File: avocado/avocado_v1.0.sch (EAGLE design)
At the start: 35 parts, among them IC1 TM4C129XXXPDT, IC2 OP-AMP

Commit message: finished wiring MCU
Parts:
- added C15: 3300pF, SparkFun-Capacitors:1.0UF-0805-25V-(+80/-20%)
- added C16, C17, C18, C19, C20, C26, C27, C28, C29, C30: 0.1uF, SparkFun-Capacitors:1.0UF-0805-25V-10%
- added C21: 2.2uF, SparkFun-Capacitors:1.0UF-0805-25V-10%
- added C22, C23, C24, C25: 12pF, SparkFun-Capacitors:1.0UF-0805-25V-10%
- added D1: GREEN, SparkFun-LED:LED-GREEN0603
- added R12, R22: 1M, rcl:R-US_R0805
- added R13, R17: 100, rcl:R-US_R0805
- added R14: 2K, rcl:R-US_R0805
- added R18: 10K, rcl:R-US_R0805
- added R21: 51, rcl:R-US_R0805
- added R23: 0, rcl:R-US_R0805
- added R24: 4.87K 1%, rcl:R-US_R0805
- added R25: (no value), rcl:R-US_R0805
- added R26: 330, rcl:R-US_R0805
- added RESET, WAKE: B3S-10XX, avocado:B3S-10XX
- added U$7: MICRO-USB-RECEPTACLE47589-0001, avocado:MICRO-USB-RECEPTACLE47589-0001
- added U$8: CX3225SB, avocado:CX3225SB
- added U1: TPD4S012_DRY_6, avocado:TPD4S012_DRY_6
- added X1: (no value), avocado:CRYSTAL-4PIN
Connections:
- net N$100 renamed PB2
- net N$101 renamed PB3
- net N$106 renamed PD7
- net N$107 renamed PD6
- net N$108 renamed PD5
- net N$109 renamed PD4
- net N$11 renamed PQ0
- net N$110 renamed PE5
- net N$111 renamed PE4
- net N$113 renamed PB4
- net N$114 renamed PB5
- net N$115 renamed PP1
- net N$116 renamed PP0
- net N$117 renamed PJ1
- net N$118 renamed PJ0
- net N$12 renamed PQ1
- net N$122 renamed PN5
- net N$123 renamed PN4
- net N$124 renamed PN3
- net N$125 renamed PN2
- net N$126 renamed PN1
- net N$127 renamed PN0
- net N$128 renamed PP5
- net N$129 renamed PP4
- net N$130 renamed PP3
- net N$131 renamed PP2
- net N$132 renamed PQ4
- net N$134 renamed SWCLK
- net N$135 renamed SWDIO
- net N$136 renamed TDI
- net N$137 renamed SWO
- net N$17 renamed PQ2
- net N$2 renamed PD0
- net N$21 renamed PE3
- net N$22 renamed PE2
- net N$23 renamed PE1
- net N$24 renamed PE0
- net N$27 renamed PK0
- net N$28 renamed PK1
- net N$29 renamed PK2
- net N$30 renamed PK3
- net N$31 renamed PC7
- net N$32 renamed PC6
- net N$33 renamed PC5
- net N$34 renamed PC4
- net N$36 renamed PQ3
- net N$38 renamed PH0
- net N$39 renamed PH1
- net N$4 renamed PD1
- net N$40 renamed PH2
- net N$41 renamed PH3
- net N$42 renamed PA0
- net N$43 renamed PA1
- net N$44 renamed PA2
- net N$45 renamed PA3
- net N$46 renamed PA4
- net N$47 renamed PA5
- net N$49 renamed PA6
- net N$50 renamed PA7
- net N$51 renamed PF0
- net N$52 renamed PF1
- net N$53 renamed PF2
- net N$54 renamed PF3
- net N$55 renamed PF4
- net N$58 renamed PG0
- net N$59 renamed PG1
- net N$6 renamed PD2
- net N$62 renamed EN0RXIN
- net N$63 renamed EN0RXIP
- net N$65 renamed EN0TXON
- net N$66 renamed EN0TXOP
- net N$69 renamed PK7
- net N$70 renamed PK6
- net N$71 renamed PK5
- net N$72 renamed PK4
- net N$74 renamed NHIB
- net N$80 renamed PM7
- net N$81 renamed PM6
- net N$82 renamed PM5
- net N$83 renamed PM4
- net N$84 renamed PM3
- net N$85 renamed PM2
- net N$86 renamed PM1
- net N$87 renamed PM0
- net N$9 renamed PD3
- net N$90 renamed PL0
- net N$91 renamed PL1
- net N$92 renamed PL2
- net N$93 renamed PL3
- net N$94 renamed PL4
- net N$95 renamed PL5
- removed net N$102: IC1.PL7
- removed net N$103: IC1.PL6
- removed net N$104: IC1.PB0
- removed net N$112: IC1.VDD@11
- removed net N$119: IC1.VDDC@1
- removed net N$120: IC1.GND@5
- removed net N$121: IC1.VDD@12
- removed net N$13: IC1.VDD@10
- removed net N$133: IC1.VDD@13
- removed net N$14: IC1.VDDA
- removed net N$15: IC1.VREFA+
- removed net N$16: IC1.GNDA
- removed net N$25: IC1.VDD@9
- removed net N$26: IC1.GND@4
- removed net N$35: IC1.VDD@8
- removed net N$37: IC1.VDD@7
- removed net N$48: IC1.VDD@6
- removed net N$56: IC1.VDD@5
- removed net N$57: IC1.GND@3
- removed net N$60: IC1.VDD@4
- removed net N$61: IC1.VDD@3
- removed net N$64: IC1.GND@2
- removed net N$67: IC1.GND@1
- removed net N$73: IC1.!WAKE
- removed net N$75: IC1.XOSC0
- removed net N$76: IC1.XOSC1
- removed net N$77: IC1.VBAT
- removed net N$78: IC1.VDD@2
- removed net N$79: IC1.!RST
- removed net N$88: IC1.VDD@1
- removed net N$89: IC1.GND
- removed net N$96: IC1.VDDC
- removed net N$97: IC1.OSC0
- removed net N$98: IC1.OSC1
- removed net N$99: IC1.VDD
- new net N$2: D1.C, R26.2
- new net N$42: C25.2
- new net N$43: R13.1, RESET.P, RESET.P1
- new net N$44: R21.1, R22.2, R23.1
- new net N$45: C24.1, R14.2, U$8.P$2
- new net N$47: C15.1, R12.2, U$7.GND1, U$7.GND2, U$7.GND3, U$7.GND4
- new net NRST: C17.1, IC1.!RST, R13.2, R18.1
- new net NWAKE: IC1.!WAKE, R22.1, WAKE.P, WAKE.P1
- new net OSC0: C25.1, IC1.OSC0, U$8.P$1
- new net OSC1: IC1.OSC1, R14.1
- new net PB0: IC1.PB1, R17.2
- new net TARGET_ID: R17.1, U$7.4, U1.D-
- new net TARGET_VBUS: IC1.PB0, U$7.1, U1.VBUS
- new net USBD_N: IC1.PL7, U$7.2, U1.D+
- new net USBD_P: IC1.PL6, U$7.3, U1.ID
- new net VBAT: C16.1, IC1.VBAT, R21.2
- new net VDDC: C21.1, C29.2, IC1.VDDC, IC1.VDDC@1
- new net VREFA: IC1.VREFA+, R25.1
- new net XOSC0: C22.1, IC1.XOSC0, X1.1
- new net XOSC1: C23.1, IC1.XOSC1, X1.4
- net 3V3DC: now also C18.1, C19.1, C20.1, C26.1, C27.2, C28.2, C30.1, D1.A, IC1.VDD, IC1.VDD@1, IC1.VDD@10, IC1.VDD@11, IC1.VDD@12, IC1.VDD@13, IC1.VDD@2, IC1.VDD@3, IC1.VDD@4, IC1.VDD@5, IC1.VDD@6, IC1.VDD@7, IC1.VDD@8, IC1.VDD@9, IC1.VDDA, R18.2, R23.2, R25.2
- net GND: now also C15.2, C16.2, C17.2, C18.2, C19.2, C20.2, C21.2, C22.2, C23.2, C24.2, C26.2, C27.1, C28.1, C29.1, C30.2, IC1.GND, IC1.GND@1, IC1.GND@2, IC1.GND@3, IC1.GND@4, IC1.GND@5, IC1.GNDA, R12.1, R24.1, R26.1, RESET.S, RESET.S1, U$7.5, U1.GND, WAKE.S, WAKE.S1
- net N$105: now also U1.N.C.; no longer IC1.PB1
- net N$68: now also R24.2
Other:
- note added: "Allen Tang Wildcat Robot Design Studio"
- note added: "BUTTONS"
- note added: "MCU"
- note added: "MOTOR"
- note added: "OSCILLATORS"
- note added: "POWER"
- note added: "USB"
- moved on the sheet: C1, C2, C3, C4, IC1, U$1, U$2

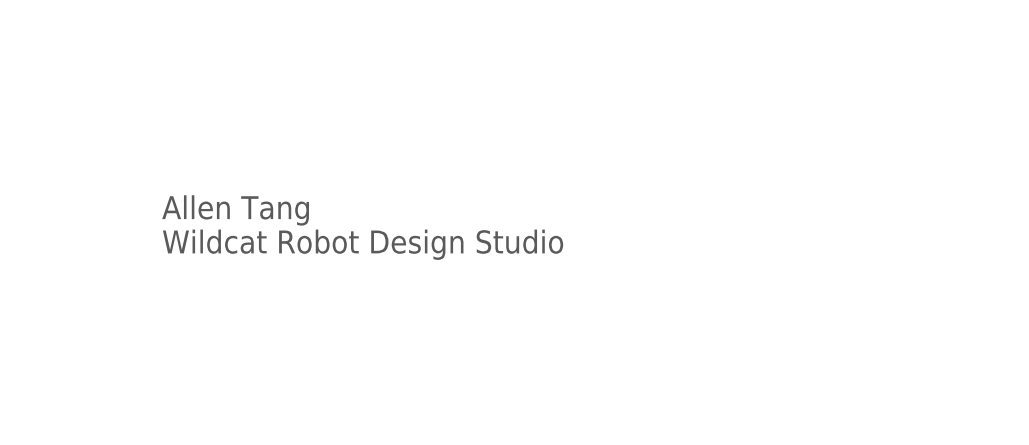
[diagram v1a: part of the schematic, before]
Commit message: fixed the title block
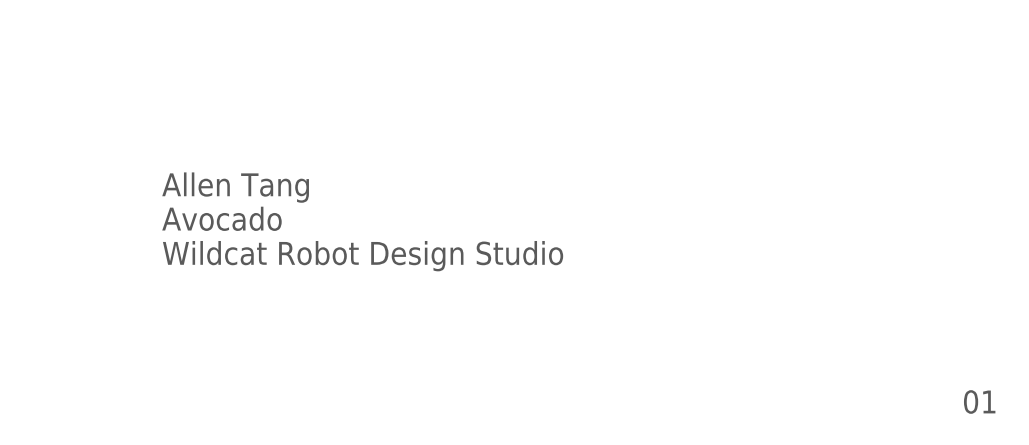
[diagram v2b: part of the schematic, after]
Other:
- note added: "01"
- note added: "Allen Tang Avocado Wildcat Robot Design Studio"
- note removed: "Allen Tang Wildcat Robot Design Studio"
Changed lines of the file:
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@@
 <wire x1="190.5" y1="81.28" x2="83.82" y2="81.28" width="0.1524" layer="97"/>
 <text x="86.36" y="78.74" size="1.778" layer="97">USB</text>
-<text x="152.4" y="-220.98" size="2.54" layer="97">Allen Tang
+<text x="152.4" y="-222.25" size="2.54" layer="97">Allen Tang
+Avocado
 Wildcat Robot Design Studio</text>
+<text x="241.3" y="-238.76" size="2.54" layer="97">01</text>
 </plain>
 <instances>

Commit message: added power and encoder block
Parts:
- removed R26: 330, rcl:R-US_R0805
- removed U$1: TLV70233DBVR, avocado:TLV70233DBVR
- removed U$2: UA78M05CDCYR, avocado:UA78M05CDCYR
- added 3V3BUCK, 5VBUCK: LM2594M-5.0, avocado:LM2594M-5.0
- added C31: 2.2uF, SparkFun-Capacitors:1.0UF-0805-25V-10%
- added C32: 1uF, SparkFun-Capacitors:1.0UF-0805-25V-10%
- added C33: 10uF, adafruit:C-USC0805K
- added C35: 0.01µF, microbuilder:CAP_CERAMIC_0805
- added D2: 1n4148, adafruit:DIODESOD-323F
- added D3: 1N4148, adafruit:DIODESOD-323F
- added D4: MBRS130LT3, avocado:MBRS130LT3
- added FB1, FB2: Ferrite, microbuilder:FERRITE_0805
- added IC3: MAX31855, adafruit:MAX6675
- added IC4: ISO3088ISO3088, avocado:ISO3088ISO3088
- added J1: 1X2-3.5MM, adafruit:1X2-3.5MM
- added OPTBIT0, OPTBIT1, OPTBIT2, OPTBIT3: (no value), avocado:QRE1113
- added R19, R27, R29, R31: 100, rcl:R-US_R0805
- added R20, R28, R30, R32: 10K, rcl:R-US_R0805
- added R33, R34: 10K, adafruit:R-US_R0805
- added SRU1028-101Y, SRU1028-151Y: SRU1028, avocado:SRU1028
- added U2: AS5048A-HTSP-500, avocado:AS5048A-HTSP-500
- C1: value 1.0uF -> 100u; device SparkFun-Capacitors:1.0UF-0805-25V-(+80/-20%) -> avocado:AVX_TPS_CAPD
- C2: value 0.33µF -> 15u; device SparkFun-Capacitors:0.33UF/330NF-0805-50V-10% -> avocado:AVX_TPS_CAPD
- C3: value 0.1uF -> 100u; device SparkFun-Capacitors:1.0UF-0805-25V-(+80/-20%) -> avocado:AVX_TPS_CAPD
- C4: value 0.1uF -> 15u; device SparkFun-Capacitors:1.0UF-0805-25V-(+80/-20%) -> avocado:AVX_TPS_CAPD
- D1: value GREEN -> MBRS130LT3; device SparkFun-LED:LED-GREEN0603 -> avocado:MBRS130LT3
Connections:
- removed net N$2: D1.C, R26.2
- removed net N$3: U$1.NC
- new net +3V3: C33.1, IC3.VCC, R33.1, R34.1
- new net CS: D3.A, IC3./CS, R34.2
- new net N$12: OPTBIT1.A, R29.1
- new net N$13: FB1.P$1, J1.2
- new net N$14: OPTBIT0.A, R31.1
- new net N$15: C35.P$1, FB1.P$2, IC3.T-
- new net N$16: FB2.P$1, J1.1
- new net N$17: C35.P$2, FB2.P$2, IC3.T+
- new net N$24: 5VBUCK.OUT, D1.C, SRU1028-151Y.1
- new net N$25: 3V3BUCK.OUT, D4.C, SRU1028-101Y.1
- new net N$26: IC4.A
- new net N$30: IC4.VCC2
- new net N$31: IC4.GND2@15
- new net N$32: IC4.B
- new net N$34: IC4.GND2@10
- new net N$35: IC4.GND2@9
- new net N$4: OPTBIT3.A, R19.1
- new net N$9: OPTBIT2.A, R27.1
- new net SCK: D2.A, IC3.SCK, R33.2
- net 24VDC: now also 3V3BUCK.VIN, 5VBUCK.VIN, C2.A, C4.A; no longer C2.1, U$2.VIN
- net 3V3DC: now also 3V3BUCK.FB, C3.A, C31.1, C32.1, IC4.VCC1, R19.2, R20.2, R27.2, R28.2, R29.2, R30.2, R31.2, R32.2, SRU1028-101Y.2, U2.VDD3V, U2.VDD5V; no longer C4.1, D1.A, U$1.VOUT
- net 5VDC: now also 5VBUCK.FB, C1.A, SRU1028-151Y.2; no longer C1.1, C3.1, U$1.VIN, U$2.VOUT
- net GND: now also 3V3BUCK.GND, 3V3BUCK.ON/OFF, 5VBUCK.GND, 5VBUCK.ON/OFF, C1.C, C2.C, C3.C, C31.2, C32.2, C33.2, C4.C, D1.A, D4.A, IC3.GND, IC4.GND1@2, IC4.GND1@7, IC4.GND1@8, OPTBIT0.E, OPTBIT0.K, OPTBIT1.E, OPTBIT1.K, OPTBIT2.E, OPTBIT2.K, OPTBIT3.E, OPTBIT3.K, U2.GND; no longer C1.2, C2.2, C3.2, C4.2, R26.1, U$1.GND, U$2.GND
- net PA2: now also U2.CLK
- net PA3: now also U2.!CSN
- net PA4: now also U2.MOSI
- net PA5: now also U2.MISO
- net PB4: now also D3.C
- net PB5: now also D2.C
- net PC4: now also IC4.R
- net PC5: now also IC4.D
- net PC6: now also IC4.!RE, IC4.DE
- net PE0: now also OPTBIT0.C, R32.1
- net PE1: now also OPTBIT1.C, R30.1
- net PE2: now also OPTBIT2.C, R28.1
- net PE3: now also OPTBIT3.C, R20.1
- net PE4: now also IC3.DO
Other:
- note added: "ENCODER"
- note added: "RS485"
- note added: "TEMPERATURE"
- moved on the sheet: C10, C11, C12, C13, C14, C15, C16, C17, C18, C19, C20, C21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

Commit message: updated motor block, power and temperature
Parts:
- removed C10: 33nF, SparkFun-Capacitors:1.0UF-0805-25V-10%
- removed C11: 5.6nF, SparkFun-Capacitors:1.0UF-0805-25V-10%
- removed C12, C7: 220nF, SparkFun-Capacitors:1.0UF-0805-25V-10%
- removed C13, C9: 10nF, SparkFun-Capacitors:1.0UF-0805-25V-10%
- removed C14, C6: 100nF, SparkFun-Capacitors:1.0UF-0805-25V-10%
- removed C15: 3300pF, SparkFun-Capacitors:1.0UF-0805-25V-(+80/-20%)
- removed C5: 100uF, SparkFun-Capacitors:100UF-POLAR-RADIAL-2.5MM-25V-20%
- removed C8: 1nF, SparkFun-Capacitors:1.0UF-0805-25V-10%
- removed IC2: OP-AMP, SparkFun-IC-Amplifiers:OPAMP-DUALDIP
- removed R10: 47K, rcl:R-US_R0805
- removed R11, R15, R16: 10, rcl:R-US_R0805
- removed R12: 1M, rcl:R-US_R0805
- removed R17, R7: 100, rcl:R-US_R0805
- removed R4: 1.8K, rcl:R-US_R0805
- removed R5: 100K, rcl:R-US_R0805
- removed R6: 1K, rcl:R-US_R0805
- removed R8: 0.6, rcl:R-US_R0805
- removed R9: 33K, rcl:R-US_R0805
- removed U$4: EC45FLAT_BLDC, avocado:EC45FLAT_BLDC
- removed U$6: 1N4148, avocado:1N4148
- removed U$7: MICRO-USB-RECEPTACLE47589-0001, avocado:MICRO-USB-RECEPTACLE47589-0001
- added CAP-0001, CAP-1114, CAP-1115, CAP-1116, CAP-1117, CAP-1118: 10nF, SparkFun-Capacitors:0.1UF-16V(+-10%)(0402)
- added CAP-0002, CAP-0119: 0.1uF, SparkFun-Capacitors:1.0UF-25V-+80/-20(0805)"
- added CAP-0003: 100nF, SparkFun-Capacitors:0.1UF-16V(+-10%)(0402)
- added CAP-0114: 1uF, SparkFun-Capacitors:2.2UF-25V-+80/-20(0805)
- added CAP-0118: 1uF, SparkFun-Capacitors:1.0UF-25V-+80/-20(0805)"
- added CAP_0115: 10uF, SparkFun-Capacitors:2.2UF-25V-+80/-20(0805)
- added CAP_0116: 0.1uF, SparkFun-Capacitors:2.2UF-25V-+80/-20(0805)
- added CAP_0117: 0.047uF, SparkFun-Capacitors:1.0UF-25V-+80/-20(0805)"
- added D5: RED, SparkFun-LED:LED-RED0603
- added D6: GREEN, SparkFun-LED:LED-GREEN0603
- added D7: BLUE, SparkFun-LED:LED-BLUE0603
- added J2, J3: (no value), avocado:61200621621
- added J4: (no value), SparkFun-Connectors:CONN_07
- added RES-0001, RES-1112: 2.21 OHM, SparkFun-Resistors:0.3OHM-1/8W-1%(0805)
- added RES-0112: 1.5k, SparkFun-Resistors:0.3OHM-1/8W-1%(0805)
- added RES-0113, RES-0114, RES-0115: 0.014 Ohm, SparkFun-Resistors:0.001OHM-3W-1%(2512)3W/1%
- added RES-1111: 2.21 Ohm, SparkFun-Resistors:0.3OHM-1/8W-1%(0805)
- added RES-1125: 10kOhm, SparkFun-Resistors:0.3OHM-1/8W-1%(0805)
- added U$1, U$2: S03B-PASK-2, avocado:S03B-PASK-2
- added U$10, U$11, U$12: CSD88584Q5DC, CSD88584Q5DC:CSD88584Q5DC
- added U$9: DRV8323S_AVOCADODRV8323S_AVOCADO, motor_control:DRV8323S_AVOCADODRV8323S_AVOCADO
- added USR_SW1, USR_SW2: B3S-10XX, avocado:B3S-10XX
- R1: value 5.6K -> 100
- R2: value 1M -> 330; device rcl:R-US_R0805 -> SparkFun-Resistors:0.3OHM-0805-1/8W-1%
- R3: value 4.7K -> 330; device rcl:R-US_R0805 -> SparkFun-Resistors:0.3OHM-0805-1/8W-1%
- U$3: value L6229DTR -> EC45FLAT_BLDC; device avocado:L6229DTR -> avocado:EC45FLAT_BLDC
- U$5: value 1N4148 -> B2PS-VH; device avocado:1N4148 -> avocado:B2PS-VH
- U1: value TPD4S012_DRY_6 -> LMT87DCKT; device avocado:TPD4S012_DRY_6 -> avocado:LMT87DCKT
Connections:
- net N$68 renamed RBIAS
- removed net +3V3: C33.1, IC3.VCC, R33.1, R34.1
- removed net BRAKE: U$3.BRAKE
- removed net EN: C11.1, R5.2, U$3.DIAG, U$3.EN
- removed net ENABLE: R5.1
- removed net F/R: U$3.FWD/REV
- removed net N$10: C7.2, IC2G1.-IN, R2.2, R3.2
- removed net N$105: U1.N.C.
- removed net N$18: U$4.NC@9
- removed net N$43: R13.1, RESET.P, RESET.P1
- removed net N$47: C15.1, R12.2, U$7.GND1, U$7.GND2, U$7.GND3, U$7.GND4
- removed net N$5: C7.1, IC2G1.OUT, R1.2, R2.1
- removed net N$7: C9.1, R7.1
- removed net RCOFF: C8.1, R9.2, U$3.RCOFF
- removed net RCPUL: C13.1, R10.2, U$3.RCPULSE
- removed net SENSE: R8.2, U$3.SENSE_A, U$3.SENSE_B
- removed net TACHO: R3.1, R6.1, U$3.TACHO
- removed net TARGET_ID: R17.1, U$7.4, U1.D-
- removed net VBOOT: C12.2, U$3.VBOOT, U$6.C
- removed net VREF: C10.1, R1.1, R4.2, U$3.VREF
- removed net V_REF: C14.1, IC2G1.+IN
- new net A: IC4.A, U$1.P$1, U$2.P$1
- new net B: IC4.B, U$1.P$2, U$2.P$2
- new net ENC_CLK: J2.2, U2.CLK
- new net ENC_GND: J2.6
- new net ENC_MISO: U2.MISO
- new net ENC_MOSI: J2.3, U2.MOSI
- new net ENC_PWR: C31.1, C32.1, J2.4, U2.VDD3V, U2.VDD5V
- new net ENC_SS: J2.1, U2.!CSN
- new net GND_EXT: IC4.GND2@10, IC4.GND2@15, IC4.GND2@9, U$1.P$3, U$2.P$3
- new net N$11: CAP-0118.1, U$9.DVDD
- new net N$2: CAP-0114.2, U$9.VCP
- new net N$22: CAP-0119.2, U$9.VREF
- new net N$23: RES-0113.2, U$10.PGND, U$9.SPC
- new net N$27: RES-0115.2, U$12.PGND, U$9.SPA
- new net N$28: CAP-1114.1, CAP-1115.1, CAP-1116.1, U$10.VIN, U$11.VIN, U$12.VIN, U$9.VDRAIN
- new net N$29: U$12.GH, U$9.GHA
- new net N$3: CAP_0117.1, U$9.CPH
- new net N$33: U$11.SH, U$9.SHB
- new net N$36: U$10.SH, U$9.SHC
- new net N$37: U$10.GL, U$9.GLC
- new net N$40: CAP-1117.2, RES-1111.2
- new net N$41: CAP-1118.2, RES-1112.2
- new net N$49: R1.2, RES-1125.1, U$9.N_FAULT
- new net N$51: J2.5
- new net N$6: CAP_0117.2, U$9.CPL
- new net NTRST: J4.7, R13.1, RESET.P, RESET.P1
- net 24VDC: now also CAP-0114.1, CAP_0115.1, CAP_0116.1, IC4.VCC2, U$5.PWR, U$9.VM; no longer C12.1, C5.+, C6.1, U$3.VS_A, U$3.VS_B, U$5.A
- net 3V3DC: now also C33.1, CAP-0002.1, CAP-0119.1, D5.A, IC3.VCC, J3.4, R3.1, R33.1, R34.1, RES-0112.1, RES-1125.2, U1.VDD; no longer C31.1, C32.1, U2.VDD3V, U2.VDD5V
- net 5VDC: now also R2.1, U$3.V_HALL; no longer R11.2, R15.2, R16.2, R6.2, U$4.V_HALL
- net GND: now also CAP-0002.2, CAP-0003.2, CAP-0118.2, CAP-1114.2, CAP-1115.2, CAP-1116.2, CAP_0115.2, CAP_0116.2, D6.C, D7.C, J3.6, RES-0001.1, RES-0113.1, RES-0114.1, RES-0115.1, RES-1111.1, RES-1112.1, U$3.GND, U$5.GND, U$9.AGND, U$9.PGND, U$9.SNA, U$9.SNB, U$9.SNC, USR_SW1.S, USR_SW1.S1, USR_SW2.S, USR_SW2.S1; no longer C10.2, C11.2, C13.2, C14.2, C15.2, C5.-, C6.2, C8.2, R10.1, R12.1, R4.1, R8.1, R9.1, U$3.GND@18, U$3.GND@19, U$3.GND@6, U$3.GND@7, U$4.GND, U$7.5
- net H1: now also U$9.INLA; no longer R16.1, U$4.H1
- net H2: now also U$3.H2, U$9.INHB; no longer R15.1, U$3.H3, U$4.H2
- net H3: now also U$3.H3, U$9.INLB; no longer R11.1, U$3.H2, U$4.H3
- net M1: now also CAP-0001.1, U$12.VSW, U$3.M1; no longer U$3.OUT1, U$4.M1
- net M2: now also CAP-1118.1, U$11.VSW, U$3.M2; no longer U$3.OUT2, U$4.M2
- net M3: now also CAP-1117.1, U$10.VSW, U$3.M3; no longer U$3.OUT3, U$4.M3
- net N$1: now also CAP-0001.2, RES-0001.2; no longer C9.2, U$3.VCP
- net N$19: now also D7.A, R2.2; no longer U$4.NC@10
- net N$20: now also D6.A, R3.2; no longer U$4.NC@11
- net N$26: now also RES-0114.2, U$11.PGND, U$9.SPB; no longer IC4.A
- net N$30: now also U$12.SH, U$9.SHA; no longer IC4.VCC2
- net N$31: now also U$12.GL, U$9.GLA; no longer IC4.GND2@15
- net N$32: now also U$11.GH, U$9.GHB; no longer IC4.B
- net N$34: now also U$11.GL, U$9.GLB; no longer IC4.GND2@10
- net N$35: now also U$10.GH, U$9.GHC; no longer IC4.GND2@9
- net N$8: now also D5.C, R1.1; no longer R7.2, U$5.C, U$6.A
- net PA0: now also J4.2
- net PA1: now also J4.1
- net PA2: now also J3.2; no longer U2.CLK
- net PA3: now also J3.1; no longer U2.!CSN
- net PA4: now also J3.3; no longer U2.MOSI
- net PA5: now also J3.5; no longer U2.MISO
- net PB0: no longer R17.2
- net PC6: no longer IC1.PC6
- net PC7: now also IC1.PC6
- net PD0: now also RES-0112.2, U$9.SDO
- net PD1: now also U$9.SDI
- net PD2: now also U$9.N_SCS
- net PD3: now also U$9.SCLK
- net PD4: now also CAP-0003.1, U1.OUT
- net PD5: now also U$9.SOC
- net PD6: now also U$9.SOB
- net PD7: now also U$9.SOA
- net PF3: now also U$9.INLC
- net PF4: now also U$9.INHC
- net PG0: now also U$9.INHA
- net PJ0: now also USR_SW1.P, USR_SW1.P1
- net PJ1: now also USR_SW2.P, USR_SW2.P1
- net PQ0: now also U$9.CAL
- net PQ1: now also U$9.ENABLE
- net SWCLK: now also J4.3
- net SWDIO: now also J4.4
- net SWO: now also J4.6
- net TARGET_VBUS: no longer U$7.1, U1.VBUS
- net TDI: now also J4.5
- net USBD_N: no longer U$7.2, U1.D+
- net USBD_P: no longer U$7.3, U1.ID
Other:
- note added: "DEBUG"
- note removed: "USB"
- moved on the sheet: 3V3BUCK, 5VBUCK, C1, C16, C17, C2, C22, C23, C24, C25, C3, C31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

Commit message: cleaned up the parts for the schematic
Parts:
- removed CAP-0001, CAP-1114, CAP-1115, CAP-1116, CAP-1117, CAP-1118: 10nF, SparkFun-Capacitors:0.1UF-16V(+-10%)(0402)
- removed CAP-0002, CAP-0119: 0.1uF, SparkFun-Capacitors:1.0UF-25V-+80/-20(0805)"
- removed CAP-0003: 100nF, SparkFun-Capacitors:0.1UF-16V(+-10%)(0402)
- removed CAP-0114: 1uF, SparkFun-Capacitors:2.2UF-25V-+80/-20(0805)
- removed CAP-0118: 1uF, SparkFun-Capacitors:1.0UF-25V-+80/-20(0805)"
- removed CAP_0115: 10uF, SparkFun-Capacitors:2.2UF-25V-+80/-20(0805)
- removed CAP_0116: 0.1uF, SparkFun-Capacitors:2.2UF-25V-+80/-20(0805)
- removed CAP_0117: 0.047uF, SparkFun-Capacitors:1.0UF-25V-+80/-20(0805)"
- removed RES-0001, RES-1112: 2.21 OHM, SparkFun-Resistors:0.3OHM-1/8W-1%(0805)
- removed RES-0112: 1.5k, SparkFun-Resistors:0.3OHM-1/8W-1%(0805)
- removed RES-0113, RES-0114, RES-0115: 0.014 Ohm, SparkFun-Resistors:0.001OHM-3W-1%(2512)3W/1%
- removed RES-1111: 2.21 Ohm, SparkFun-Resistors:0.3OHM-1/8W-1%(0805)
- removed RES-1125: 10kOhm, SparkFun-Resistors:0.3OHM-1/8W-1%(0805)
- removed U$8: CX3225SB, avocado:CX3225SB
- removed X1: (no value), avocado:CRYSTAL-4PIN
- added C10, C13: 1uF, rcl:C-USC0805
- added C11: 0.047uF, rcl:C-USC0805
- added C12, C36, C8: 0.1uF, rcl:C-USC0805
- added C14, C15, C34, C5, C6, C7: 10nF, rcl:C-USC0402
- added C37: 0.01uF, rcl:C-USC0805
- added C9: 10uF, rcl:C-USC0805
- added R10, R11, R9: 0.014, rcl:R-US_R2512
- added R4, R5, R6: 2.21, rcl:R-US_R0805
- added R7: 10K, rcl:R-US_R0805
- added R8: 1.5K, rcl:R-US_R0805
- added U$4: NX3225GA, avocado:NX3225GA
- added X2: (no value), avocado:CRYSTAL-ABS07
- C16, C17, C18, C20, C22, C23, C24, C25, C26, C27, C28, C29, C32: device SparkFun-Capacitors:1.0UF-0805-25V-10% -> rcl:C-USC0805
- C19: value 0.1uF -> 10uF; device SparkFun-Capacitors:1.0UF-0805-25V-10% -> rcl:C-USC0805
- C21: value 2.2uF -> 0.1uF; device SparkFun-Capacitors:1.0UF-0805-25V-10% -> rcl:C-USC0805
- C30: value 0.1uF -> 2.2uF; device SparkFun-Capacitors:1.0UF-0805-25V-10% -> rcl:C-USC0805
- C31: value 2.2uF -> 1uF; device SparkFun-Capacitors:1.0UF-0805-25V-10% -> rcl:C-USC0805
- C33: value 10uF -> 0.1uF; device adafruit:C-USC0805K -> rcl:C-USC0805
- C35: value 0.01µF -> 0.01uF; device microbuilder:CAP_CERAMIC_0805 -> rcl:C-USC0805
- IC4: value ISO3088ISO3088 -> ISO3088; device avocado:ISO3088ISO3088 -> avocado:ISO3088
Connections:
- removed net N$28: CAP-1114.1, CAP-1115.1, CAP-1116.1, U$10.VIN, U$11.VIN, U$12.VIN, U$9.VDRAIN
- new net N$5: C5.1, C6.1, C7.1, U$10.VIN, U$11.VIN, U$12.VIN, U$9.VDRAIN
- net 24VDC: now also C10.1, C8.1, C9.1; no longer CAP-0114.1, CAP_0115.1, CAP_0116.1
- net 3V3DC: now also C12.1, C27.1, C28.1, C36.1, R7.2, R8.2; no longer C27.2, C28.2, C30.1, CAP-0002.1, CAP-0119.1, RES-0112.1, RES-1125.2
- net GND: now also C13.2, C25.2, C27.2, C28.2, C29.2, C35.2, C36.2, C5.2, C6.2, C7.2, C8.2, C9.2, R10.1, R11.1, R4.1, R5.1, R6.1, R9.1; no longer C22.2, C27.1, C28.1, C29.1, CAP-0002.2, CAP-0003.2, CAP-0118.2, CAP-1114.2, CAP-1115.2, CAP-1116.2, CAP_0115.2, CAP_0116.2, RES-0001.1, RES-0113.1, RES-0114.1, RES-0115.1, RES-1111.1, RES-1112.1
- net M1: now also C34.1, U$3.M1@1, U$3.M1@2; no longer CAP-0001.1, U$3.M1
- net M2: now also C15.1, U$3.M2@1, U$3.M2@2; no longer CAP-1118.1, U$3.M2
- net M3: now also C14.1, U$3.M3@1, U$3.M3@2; no longer CAP-1117.1, U$3.M3
- net N$1: now also C34.2, R6.2; no longer CAP-0001.2, RES-0001.2
- net N$11: now also C13.1; no longer CAP-0118.1
- net N$15: now also C37.1; no longer C35.P$1
- net N$17: now also C37.2; no longer C35.P$2
- net N$2: now also C10.2; no longer CAP-0114.2
- net N$22: now also C12.2; no longer CAP-0119.2
- net N$23: now also R11.2; no longer RES-0113.2
- net N$26: now also R10.2; no longer RES-0114.2
- net N$27: now also R9.2; no longer RES-0115.2
- net N$3: now also C11.1; no longer CAP_0117.1
- net N$40: now also C14.2, R4.2; no longer CAP-1117.2, RES-1111.2
- net N$41: now also C15.2, R5.2; no longer CAP-1118.2, RES-1112.2
- net N$42: now also C22.2, U$4.P$3; no longer C25.2
- net N$45: now also C23.1, U$4.P$2; no longer C24.1, U$8.P$2
- net N$49: now also R7.1; no longer RES-1125.1
- net N$6: now also C11.2; no longer CAP_0117.2
- net OSC0: now also C22.1, U$4.P$1; no longer C25.1, U$8.P$1
- net PD0: now also R8.1; no longer RES-0112.2
- net PD4: now also C35.1; no longer CAP-0003.1
- net VDDC: now also C29.1, C30.1; no longer C29.2
- net XOSC0: now also C24.1, X2.P$1; no longer C22.1, X1.1
- net XOSC1: now also C25.1, X2.P$2; no longer C23.1, X1.4
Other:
- moved on the sheet: C18, C19, C20, C21, C22, C23, C24, C25, C26, C27, C28, C29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
